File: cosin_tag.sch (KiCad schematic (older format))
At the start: 65 parts, among them IC1 ATTINY13-SS, P1 ISP, Q1 2N7002, Q2 2N7002, Q3 2N7002, Q4 2N7002, Q5 2N7002

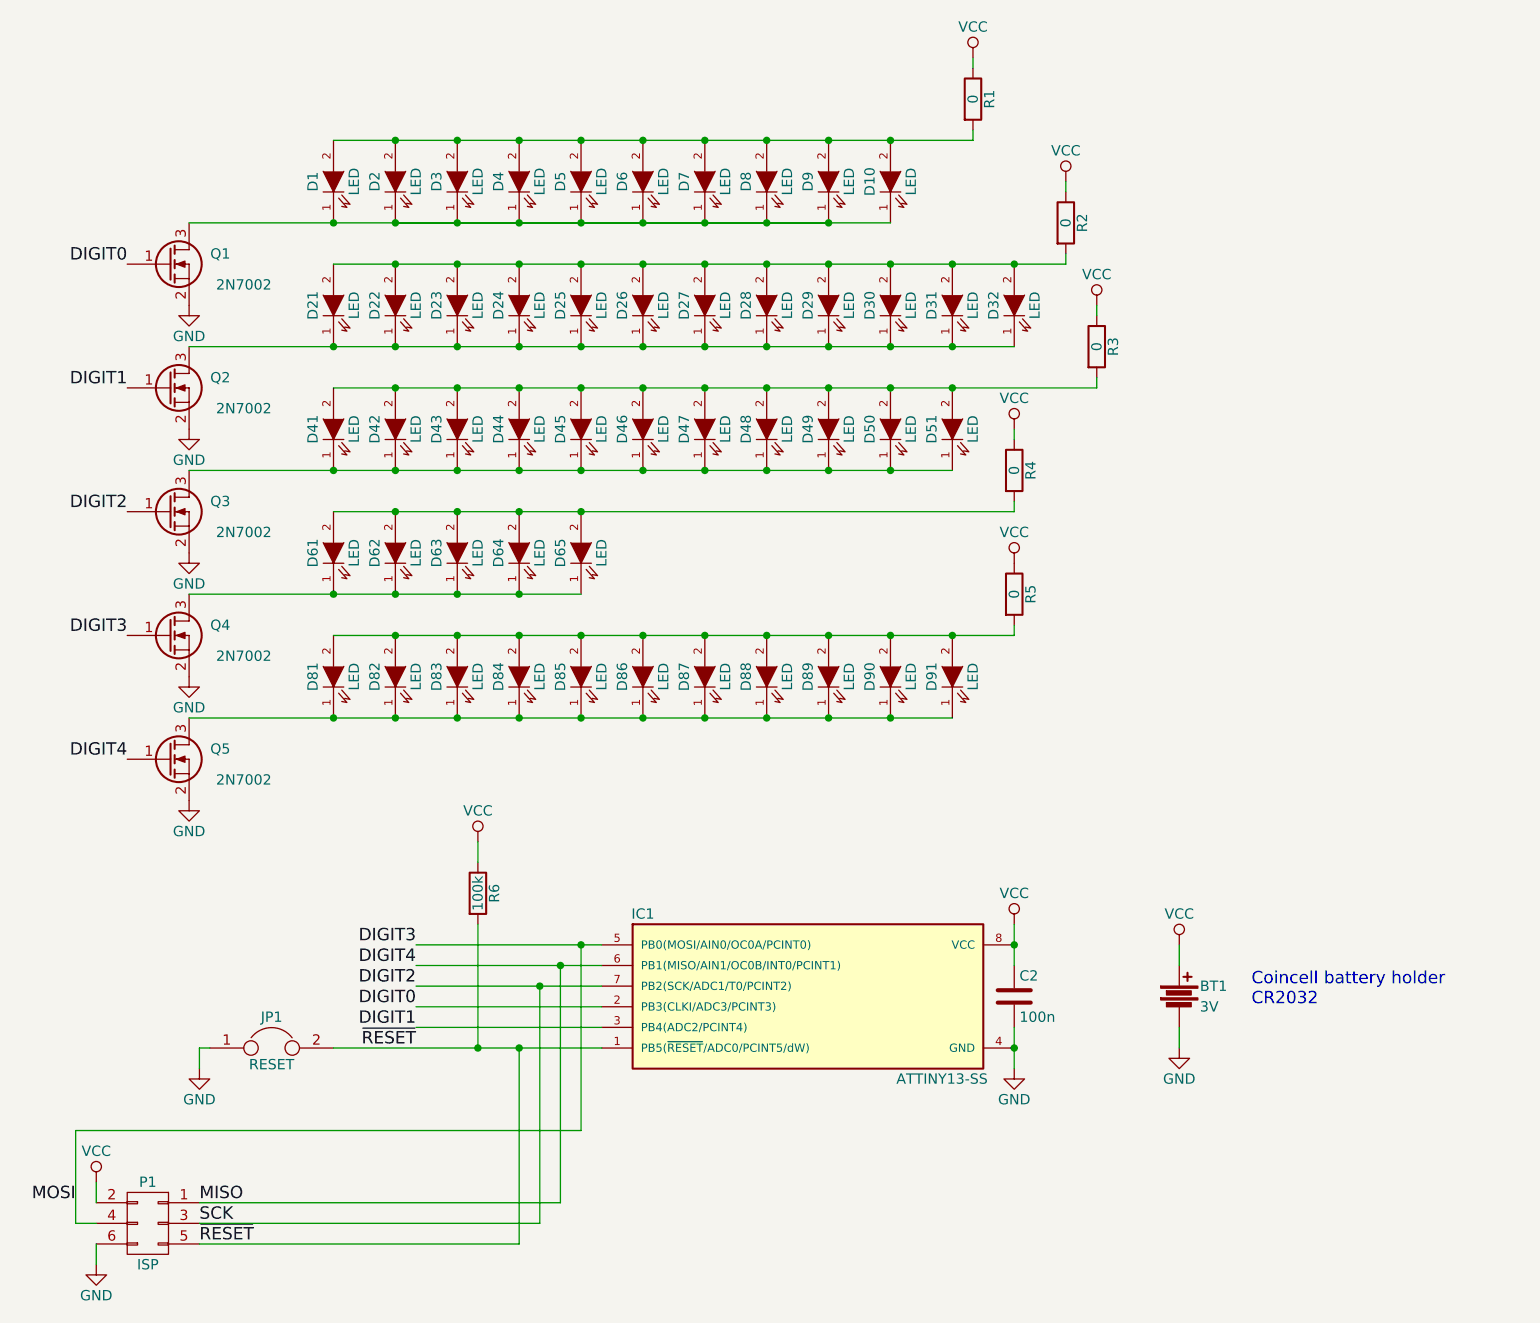
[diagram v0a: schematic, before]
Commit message: Minimized the areas in the layout where the tracks are close together. Made the tracks around the microcontroller smaller to improve yield when etching the PCB at home. For this a new netclass was introduced and the global cleareance rule is now higher. Cleaned up the values and references on the board and added a output PDF to show the placing of the components.
Added the resistor values to the schematic.

Updated all output files.
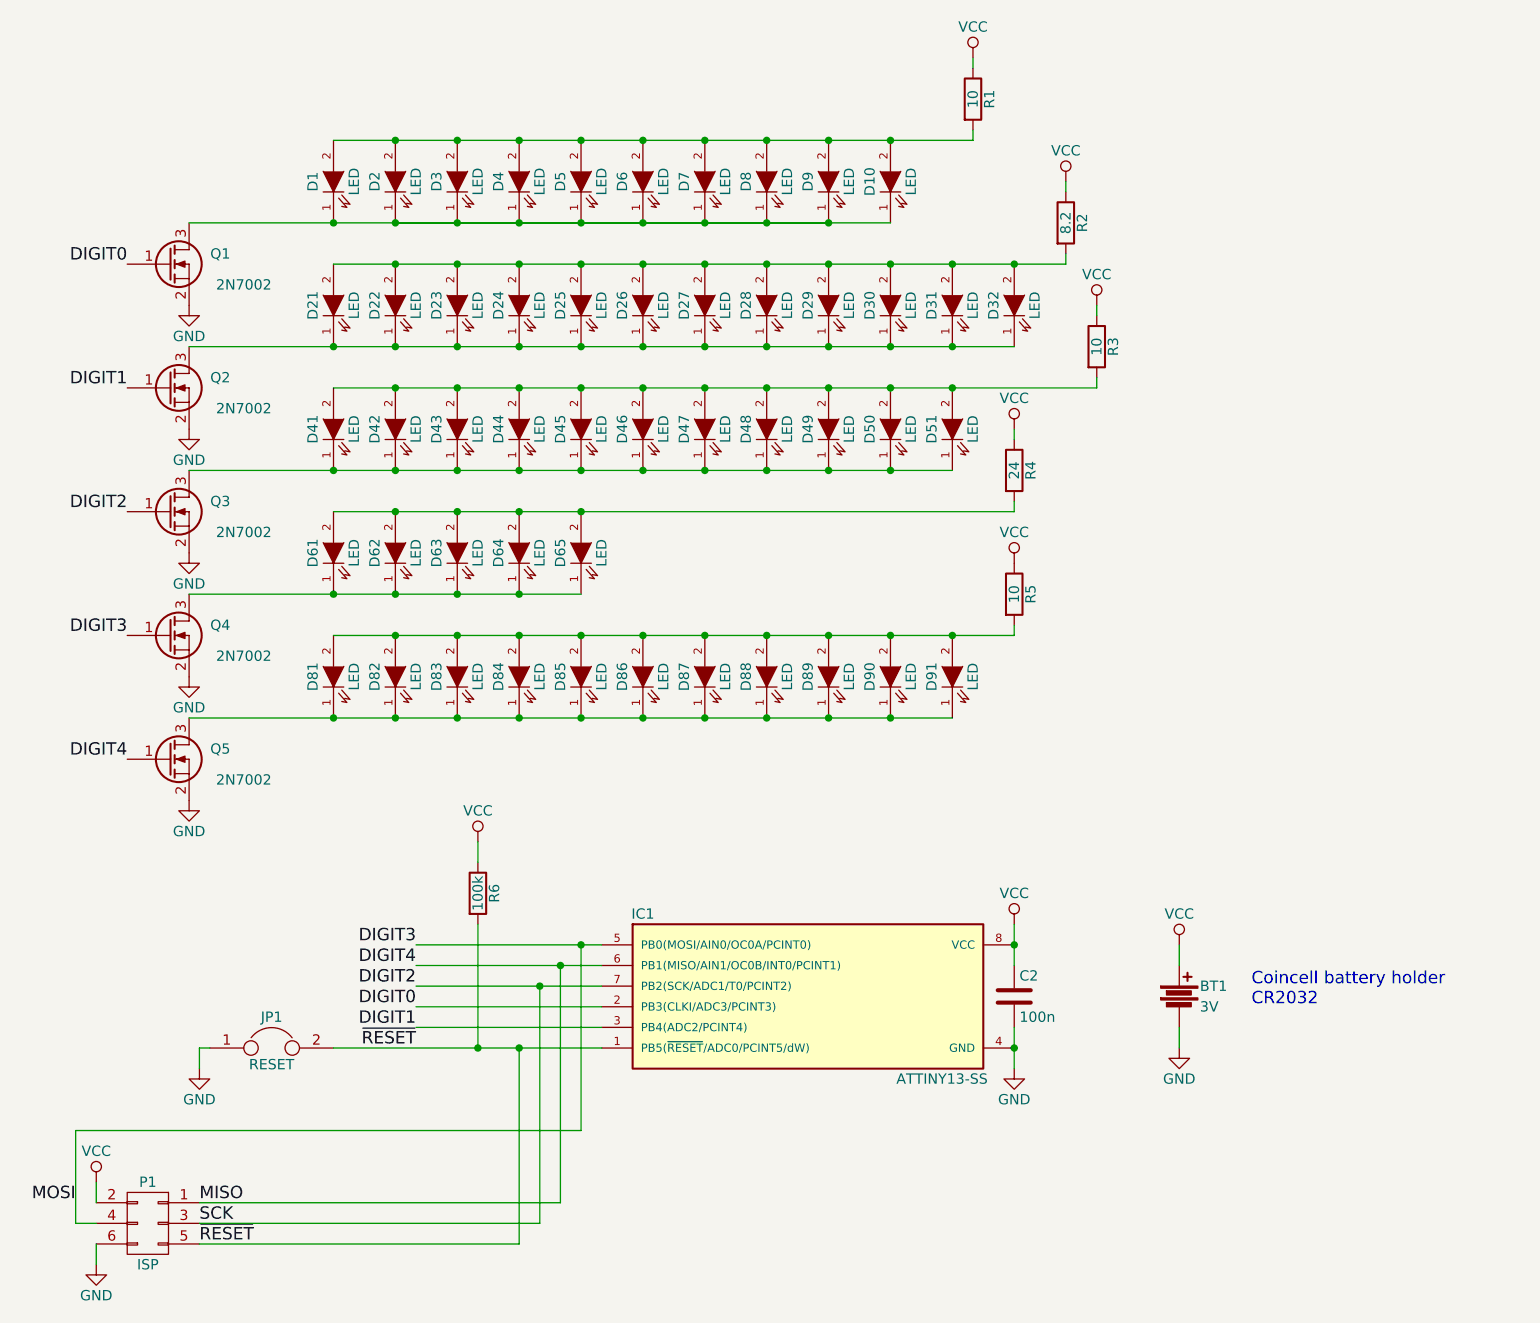
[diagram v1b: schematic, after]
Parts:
- R1, R3, R5: value 0 -> 10
- R2: value 0 -> 8.2
- R4: value 0 -> 24
